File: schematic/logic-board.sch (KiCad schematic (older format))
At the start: 80 parts

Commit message: reset bug fix
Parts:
- removed R?: 10K, ~, symbol USR
- R?: value 100K -> 47K
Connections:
- wire segments 197 -> 196
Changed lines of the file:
@@
 P 5100 6450
 F 0 "R?" V 5180 6450 40  0000 C CNN
-F 1 "100K" V 5000 6450 40  0000 C CNN
+F 1 "47K" V 5000 6450 40  0000 C CNN
 F 2 "~" V 5030 6450 30  0000 C CNN
 F 3 "~" H 5100 6450 30  0000 C CNN
@@
 	1    4850 6450
 	0    -1   -1   0
-$EndComp
-$Comp
-L USR R?
-U 1 1 57897EE5
-P 5350 5050
-F 0 "R?" V 5430 5050 40  0000 C CNN
-F 1 "10K" V 5250 5050 40  0000 C CNN
-F 2 "~" V 5280 5050 30  0000 C CNN
-F 3 "~" H 5350 5050 30  0000 C CNN
-	1    5350 5050
-	-1   0    0    1
 $EndComp
 $Comp
@@
 Connection ~ 4850 6450
 Wire Wire Line
-	5350 4800 6700 4800
+	5100 4800 6700 4800
 Wire Wire Line
 	6700 4800 6700 5000
 Connection ~ 5350 6450
-Wire Wire Line
-	5350 5300 5350 6700
-Connection ~ 5350 5300
 Connection ~ 4900 8200
 Connection ~ 4400 8200
@@
 Connection ~ 2300 5600
 Connection ~ 2300 5100
-Wire Wire Line
-	5100 4450 5100 5300
-Wire Wire Line
-	5100 5300 5350 5300
 Wire Wire Line
 	4900 4450 4350 4450
@@
 Wire Wire Line
 	12600 5050 12600 5400
+Wire Wire Line
+	5100 4450 5100 4800
+Connection ~ 5350 4800
+Wire Wire Line
+	5350 4800 5350 6700
 $EndSCHEMATC

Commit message: schematic is "done"
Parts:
- removed P?: 1-PIN_HEADER, ~, symbol 1-PIN_HEADER
- removed P?: 2-PIN_HEADER, ~, symbol 2-PIN_HEADER
- removed Q?: ZVN4206, ~, symbol MOSFET_N
- added P?: 1-PIN_HEADER, ~, symbol 1-PIN_HEADER
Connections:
- net labels added: 1Hz
- net labels removed: DISPLAY_PWM, DISPLAY_PWM_SINK
- wire segments 196 -> 192
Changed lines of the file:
@@
 $Descr A3 16535 11693
 encoding utf-8
-Sheet 3 6
+Sheet 5 8
 Title "LOGIC CLOCK LOGIC BOARD"
-Date "25 aug 2016"
+Date "28 aug 2016"
 Rev "1"
 Comp "Michael Craft"
@@
 $EndComp
 NoConn ~ 8100 6600
-$Comp
-L 1-PIN_HEADER P?
-U 1 1 57895690
-P 14300 8700
-F 0 "P?" H 14100 8700 50  0000 C CNN
-F 1 "1-PIN_HEADER" H 14300 8800 50  0001 C CNN
-F 2 "~" H 14450 8850 60  0000 C CNN
-F 3 "~" H 14450 8850 60  0000 C CNN
-	1    14300 8700
-	1    0    0    1
-$EndComp
-$Comp
-L 2-PIN_HEADER P?
-U 1 1 5789569F
-P 14750 8700
-F 0 "P?" H 14500 8700 50  0000 C CNN
-F 1 "2-PIN_HEADER" H 14750 8800 50  0001 C CNN
-F 2 "~" H 14850 8850 60  0000 C CNN
-F 3 "~" H 14850 8850 60  0000 C CNN
-	1    14750 8700
-	1    0    0    1
-$EndComp
-Text HLabel 14700 8750 3    60   Output ~ 0
-+5V
-Text HLabel 14800 8750 3    60   UnSpc ~ 0
-DISPLAY_PWM_SINK
-Text HLabel 14300 8750 3    60   Input ~ 0
-DISPLAY_PWM
-$Comp
-L +5V #PWR?
-U 1 1 57895C0C
-P 14700 8450
-F 0 "#PWR?" H 14700 8540 20  0001 C CNN
-F 1 "+5V" H 14700 8540 30  0000 C CNN
-F 2 "" H 14700 8450 60  0000 C CNN
-F 3 "" H 14700 8450 60  0000 C CNN
-	1    14700 8450
-	-1   0    0    -1
-$EndComp
-$Comp
-L MOSFET_N Q?
-U 1 1 57895CD4
-P 14300 8250
-F 0 "Q?" H 14310 8420 60  0000 R CNN
-F 1 "ZVN4206" V 14310 8100 60  0000 R CNN
-F 2 "~" H 14300 8250 60  0000 C CNN
-F 3 "~" H 14300 8250 60  0000 C CNN
-	1    14300 8250
-	0    1    -1   0
-$EndComp
-$Comp
-L GND #PWR?
-U 1 1 57895DB2
-P 14100 8150
-F 0 "#PWR?" H 14100 8150 30  0001 C CNN
-F 1 "GND" H 14100 8080 30  0001 C CNN
-F 2 "" H 14100 8150 60  0000 C CNN
-F 3 "" H 14100 8150 60  0000 C CNN
-	1    14100 8150
-	0    1    -1   0
-$EndComp
 $Comp
 L GND #PWR?
@@
 Connection ~ 15550 6600
 Connection ~ 15050 6600
-Wire Wire Line
-	15050 4700 15050 6600
-Wire Wire Line
-	12500 4700 15050 4700
 Wire Wire Line
 	12500 4700 12500 5400
@@
 Connection ~ 7450 7100
 Connection ~ 7350 7100
-Wire Notes Line
-	14600 8750 14600 9700
-Wire Notes Line
-	14900 8750 14900 9700
-Wire Wire Line
-	14300 8450 14300 8750
-Wire Wire Line
-	14700 8450 14700 8750
-Wire Wire Line
-	14800 8150 14800 8750
-Wire Notes Line
-	14900 9700 14600 9700
-Connection ~ 14700 8450
-Connection ~ 14300 8450
-Wire Wire Line
-	14500 8150 14800 8150
-Connection ~ 14800 8450
-Connection ~ 14100 8150
-Wire Notes Line
-	14200 8750 14200 9450
-Wire Notes Line
-	14200 9450 14400 9450
-Wire Notes Line
-	14400 9450 14400 8750
 Wire Wire Line
 	9000 4900 9000 5550
@@
 Wire Wire Line
 	5350 4800 5350 6700
+Text HLabel 15350 4700 2    60   Output ~ 0
+1Hz
+$Comp
+L 1-PIN_HEADER P?
+U 1 1 57C42046
+P 15300 4700
+F 0 "P?" H 15100 4700 50  0000 C CNN
+F 1 "1-PIN_HEADER" H 15300 4800 50  0001 C CNN
+F 2 "~" H 15450 4850 60  0000 C CNN
+F 3 "~" H 15450 4850 60  0000 C CNN
+	1    15300 4700
+	0    1    1    0
+$EndComp
+Wire Wire Line
+	12500 4700 15350 4700
+Wire Wire Line
+	15050 4700 15050 6600
+Connection ~ 15050 4700
+Wire Notes Line
+	15350 4600 15650 4600
+Wire Notes Line
+	15650 4600 15650 4800
+Wire Notes Line
+	15650 4800 15350 4800
 $EndSCHEMATC

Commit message: added fast set
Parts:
- added P? (x2): 3-PIN_HEADER, ~, symbol 3-PIN_HEADER
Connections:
- net labels added: 10Hz_OUT, 10Hz_OUT2, 1Hz_OUT, MIN-CARRY, SEC_CLOCK, TEN-MIN_CLOCK
- wire segments 192 -> 285
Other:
- note added: "TO FAST SET SWITCH"
- moved on the sheet: R?

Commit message: added note
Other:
- note added: "BUSSED PULLDOWN ARRAYS"
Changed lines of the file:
@@
 Text Notes 6800 8900 1    60   ~ 0
 TO FAST SET SWITCH
+Text Notes 9150 3000 0    60   ~ 0
+BUSSED PULLDOWN ARRAYS
 $EndSCHEMATC

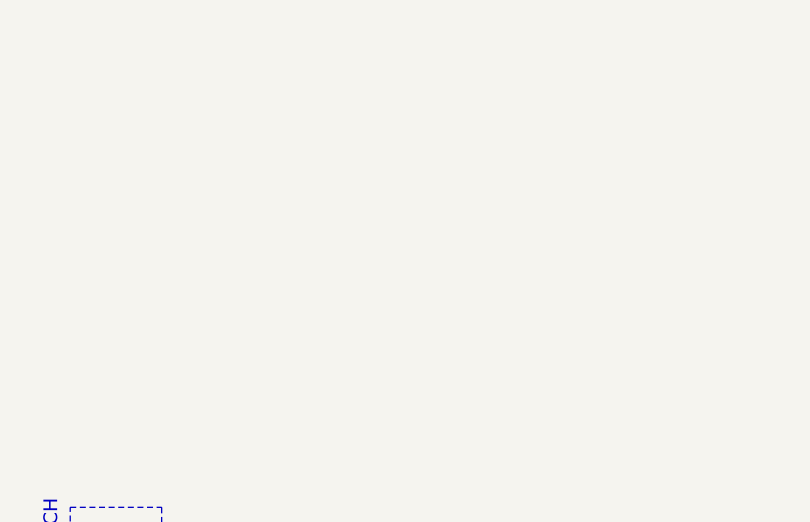
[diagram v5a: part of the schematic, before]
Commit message: started rs232 board
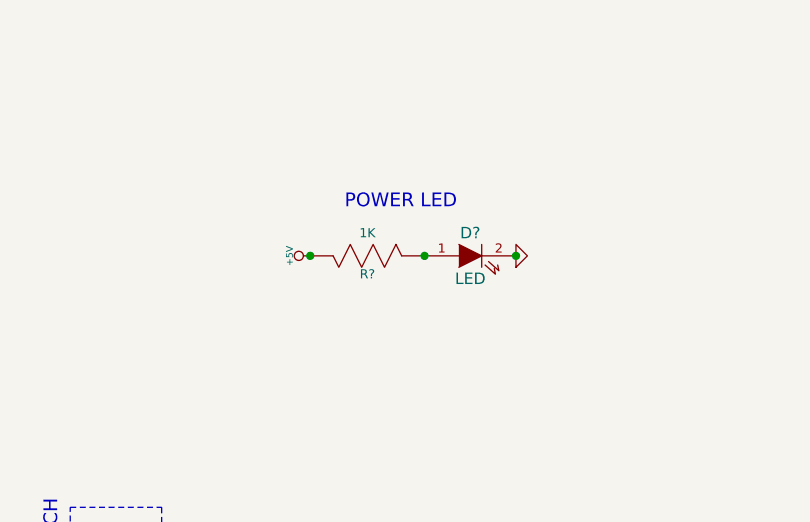
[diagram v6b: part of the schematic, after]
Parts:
- added D?: LED, ~, symbol LED
- added R?: 1K, ~, symbol USR
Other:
- note added: "POWER LED"
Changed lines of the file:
@@
 Sheet 5 8
 Title "LOGIC CLOCK LOGIC BOARD"
-Date "28 aug 2016"
+Date "29 aug 2016"
 Rev "1"
 Comp "Michael Craft"
@@
 Text Notes 9150 3000 0    60   ~ 0
 BUSSED PULLDOWN ARRAYS
+$Comp
+L LED D?
+U 1 1 57C3849D
+P 14050 2000
+F 0 "D?" H 14050 2100 50  0000 C CNN
+F 1 "LED" H 14050 1900 50  0000 C CNN
+F 2 "~" H 14050 2000 60  0000 C CNN
+F 3 "~" H 14050 2000 60  0000 C CNN
+	1    14050 2000
+	1    0    0    -1
+$EndComp
+$Comp
+L GND #PWR?
+U 1 1 57C3862A
+P 14250 2000
+F 0 "#PWR?" H 14250 2000 30  0001 C CNN
+F 1 "GND" H 14250 1930 30  0001 C CNN
+F 2 "" H 14250 2000 60  0000 C CNN
+F 3 "" H 14250 2000 60  0000 C CNN
+	1    14250 2000
+	0    -1   -1   0
+$EndComp
+Connection ~ 14250 2000
+$Comp
+L USR R?
+U 1 1 57C38870
+P 13600 2000
+F 0 "R?" V 13680 2000 40  0000 C CNN
+F 1 "1K" V 13500 2000 40  0000 C CNN
+F 2 "~" V 13530 2000 30  0000 C CNN
+F 3 "~" H 13600 2000 30  0000 C CNN
+	1    13600 2000
+	0    1    1    0
+$EndComp
+Connection ~ 13850 2000
+$Comp
+L +5V #PWR?
+U 1 1 57C3887B
+P 13350 2000
+F 0 "#PWR?" H 13350 2090 20  0001 C CNN
+F 1 "+5V" H 13350 2090 30  0000 C CNN
+F 2 "" H 13350 2000 60  0000 C CNN
+F 3 "" H 13350 2000 60  0000 C CNN
+	1    13350 2000
+	0    -1   -1   0
+$EndComp
+Connection ~ 13350 2000
+Text Notes 13500 1800 0    60   ~ 0
+POWER LED
 $EndSCHEMATC

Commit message: I HAVE NO IDEA
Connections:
- wire segments 285 -> 201

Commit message: minutes and seconds digits confirmed working, hours needs work
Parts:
- added R?: 10K, ~, symbol USR
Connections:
- wire segments 201 -> 202
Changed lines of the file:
@@
 Sheet 5 8
 Title "LOGIC CLOCK LOGIC BOARD"
-Date "2 sep 2016"
+Date "20 nov 2016"
 Rev "1"
 Comp "Michael Craft"
@@
 Wire Wire Line
 	7650 6600 7650 7400
-Wire Wire Line
-	9000 5550 8450 5550
 Connection ~ 7650 7100
 Connection ~ 7550 7100
@@
 Connection ~ 8650 6950
 Wire Wire Line
-	8450 5550 8450 6750
-Wire Wire Line
-	8450 6750 8150 6750
+	8150 6750 8550 6750
 Wire Wire Line
 	12300 4500 12300 5550
@@
 Connection ~ 9050 2400
 Connection ~ 9150 2400
+$Comp
+L USR R?
+U 1 1 5831F3F9
+P 8550 6050
+F 0 "R?" V 8630 6050 40  0000 C CNN
+F 1 "10K" V 8450 6050 40  0000 C CNN
+F 2 "~" V 8480 6050 30  0000 C CNN
+F 3 "~" H 8550 6050 30  0000 C CNN
+	1    8550 6050
+	1    0    0    -1
+$EndComp
+Wire Wire Line
+	9000 5550 8550 5550
+Wire Wire Line
+	8550 5550 8550 5800
+Wire Wire Line
+	8550 6750 8550 6300
 $EndSCHEMATC
